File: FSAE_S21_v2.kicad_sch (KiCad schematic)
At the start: 77 parts

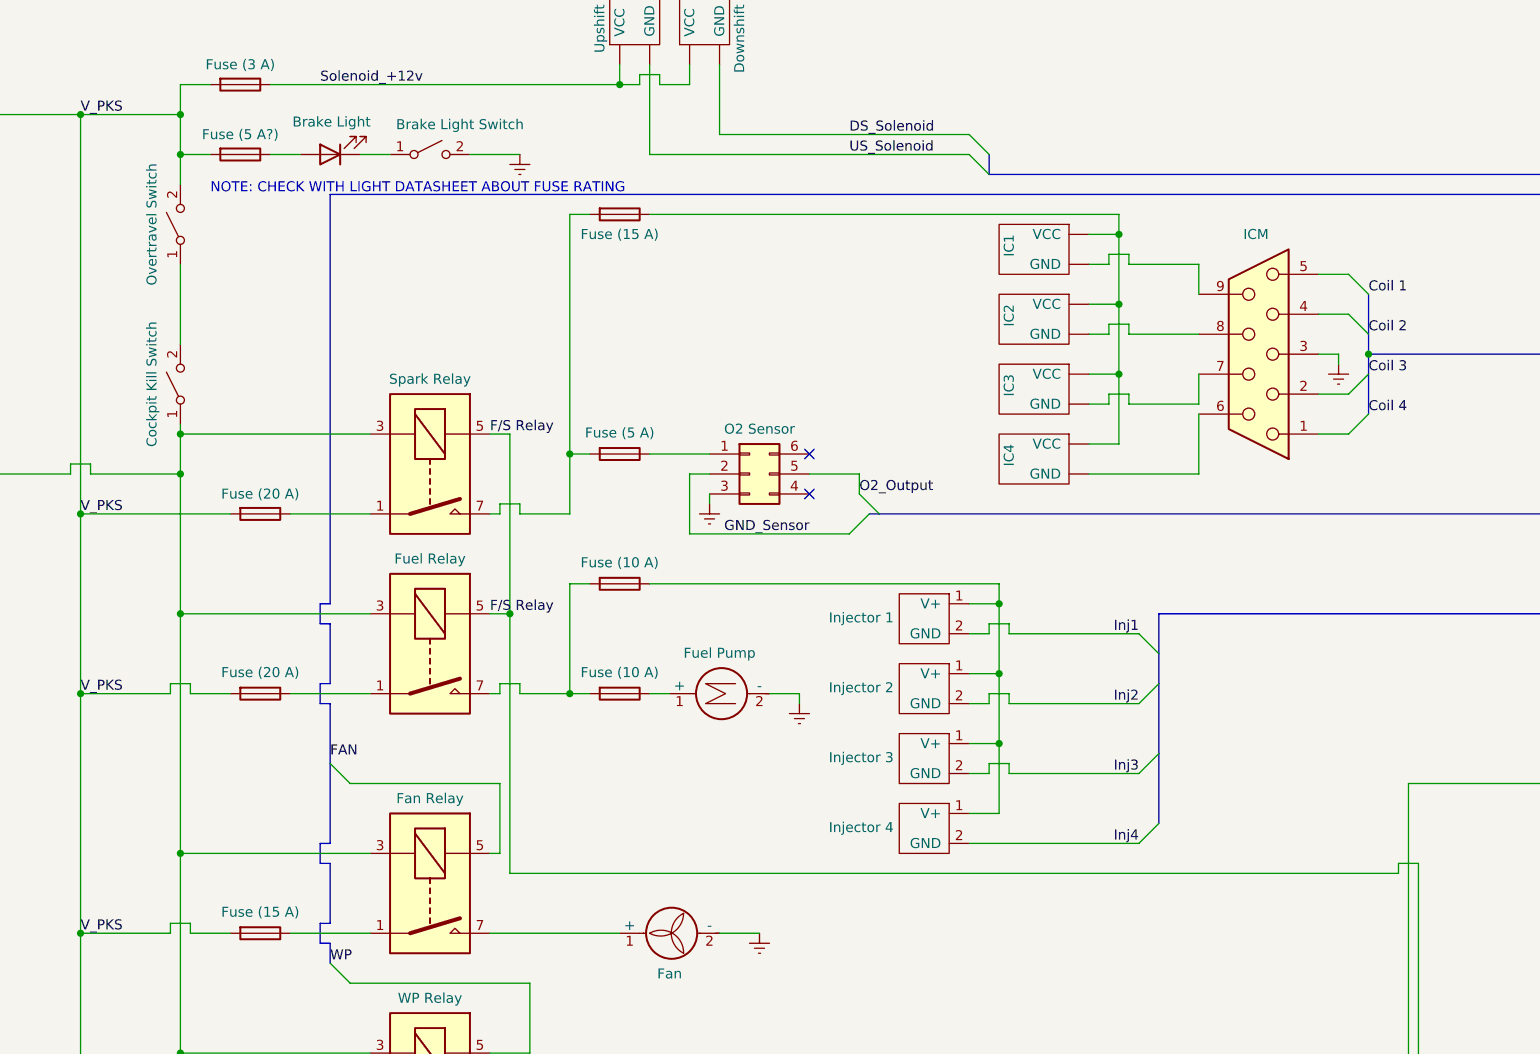
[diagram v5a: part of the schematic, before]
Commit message: fixed killswitch wiring
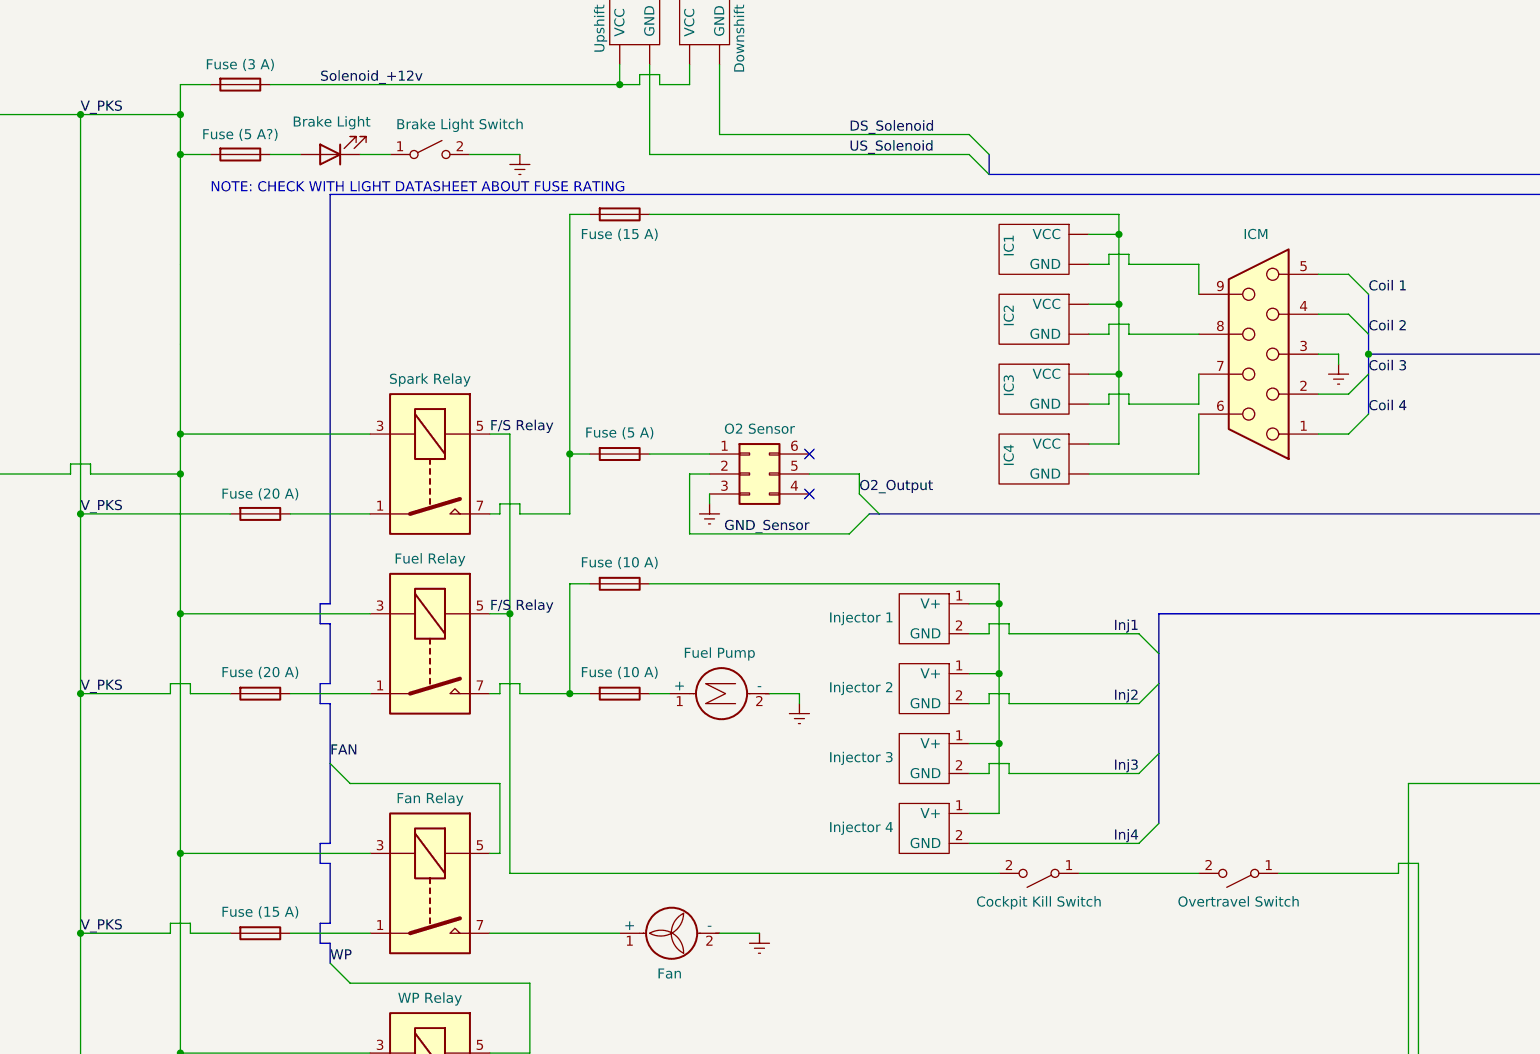
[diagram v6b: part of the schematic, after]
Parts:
- removed SW?: Cockpit Kill Switch, symbol Switch:SW_SPST
- removed SW?: Overtravel Switch, symbol Switch:SW_SPST
- added SW?: Cockpit Kill Switch, symbol Switch:SW_SPST
- added SW?: Overtravel Switch, symbol Switch:SW_SPST
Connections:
- net V_PKS is gone; now on net V_CKS: F?.2, F?.2, F?.2, F?.2, F?.2, F?.2, F?.2, F?.2, F?.2, K?.1, SW?.2 (B)
- net F/S Relay: now also SW?.1 (A), SW?.2 (B)
- new net: F?.1, U?.~ (VCC), U?.~ (VCC), U?.~ (VCC), U?.~ (VCC)
- new net: SW?.1 (A), SW?.2 (B)
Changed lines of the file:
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@@
     (stroke (width 0) (type default) (color 0 0 0 0))
   )
+  (wire (pts (xy 218.44 127) (xy 233.68 127))
+    (stroke (width 0) (type default) (color 0 0 0 0))
+  )
   (wire (pts (xy 403.86 43.18) (xy 417.83 43.18))
     (stroke (width 0) (type default) (color 0 0 0 0))
@@
     (stroke (width 0) (type default) (color 0 0 0 0))
   )
+  (wire (pts (xy 243.84 127) (xy 259.08 127))
+    (stroke (width 0) (type default) (color 0 0 0 0))
+  )
   (wire (pts (xy 441.96 58.42) (xy 441.96 62.23))
     (stroke (width 0) (type default) (color 0 0 0 0))
@@
     (stroke (width 0) (type default) (color 0 0 0 0))
   )
-  (wire (pts (xy 146.05 127) (xy 259.08 127))
+  (wire (pts (xy 146.05 127) (xy 208.28 127))
     (stroke (width 0) (type default) (color 0 0 0 0))
   )
@@
     (stroke (width 0) (type default) (color 0 0 0 0))
   )
-  (wire (pts (xy 539.75 149.86) (xy 548.64 149.86))
+  (wire (pts (xy 104.14 35.56) (xy 104.14 49.53))
     (stroke (width 0) (type default) (color 0 0 0 0))
   )
-  (wire (pts (xy 468.63 62.23) (xy 482.6 62.23))
+  (wire (pts (xy 539.75 149.86) (xy 548.64 149.86))
     (stroke (width 0) (type default) (color 0 0 0 0))
   )
-  (wire (pts (xy 104.14 35.56) (xy 104.14 39.37))
+  (wire (pts (xy 468.63 62.23) (xy 482.6 62.23))
     (stroke (width 0) (type default) (color 0 0 0 0))
   )
@@
     (stroke (width 0) (type default) (color 0 0 0 0))
   )
-  (wire (pts (xy 104.14 71.12) (xy 104.14 69.85))
+  (wire (pts (xy 104.14 59.69) (xy 104.14 71.12))
     (stroke (width 0) (type default) (color 0 0 0 0))
   )
@@
     (pin "2")
   )
-  (symbol (lib_id "Switch:SW_SPST") (at 104.14 64.77 90) (unit 1)
-    (in_bom yes) (on_board yes)
-    (property "Reference" "SW?" (id 0) (at 98.171 64.77 0)
-      (effects (font (size 1.27 1.27)) hide)
-    )
-    (property "Value" "Cockpit Kill Switch" (id 1) (at 100.5078 64.77 0))
-    (property "Footprint" "" (id 2) (at 104.14 64.77 0)
-      (effects (font (size 1.27 1.27)) hide)
-    )
-    (property "Datasheet" "~" (id 3) (at 104.14 64.77 0)
-      (effects (font (size 1.27 1.27)) hide)
-    )
-    (pin "1")
-    (pin "2")
-  )
-  (symbol (lib_id "Switch:SW_SPST") (at 104.14 44.45 90) (unit 1)
-    (in_bom yes) (on_board yes)
-    (property "Reference" "SW?" (id 0) (at 98.171 44.45 0)
-      (effects (font (size 1.27 1.27)) hide)
-    )
-    (property "Value" "Overtravel Switch" (id 1) (at 100.5078 44.45 0))
-    (property "Footprint" "" (id 2) (at 104.14 44.45 0)
-      (effects (font (size 1.27 1.27)) hide)
-    )
-    (property "Datasheet" "~" (id 3) (at 104.14 44.45 0)
-      (effects (font (size 1.27 1.27)) hide)
-    )
-    (pin "1")
-    (pin "2")
-  )
   (symbol (lib_id "Device:LED") (at 123.19 35.56 180) (unit 1)
     (in_bom yes) (on_board yes)
@@
     (pin "2")
   )
+  (symbol (lib_id "Switch:SW_SPST") (at 213.36 127 180) (unit 1)
+    (in_bom yes) (on_board yes)
+    (property "Reference" "SW?" (id 0) (at 213.36 132.969 0)
+      (effects (font (size 1.27 1.27)) hide)
+    )
+    (property "Value" "Cockpit Kill Switch" (id 1) (at 213.36 130.6322 0))
+    (property "Footprint" "" (id 2) (at 213.36 127 0)
+      (effects (font (size 1.27 1.27)) hide)
+    )
+    (property "Datasheet" "~" (id 3) (at 213.36 127 0)
+      (effects (font (size 1.27 1.27)) hide)
+    )
+    (pin "1")
+    (pin "2")
+  )
   (symbol (lib_id "Device:IC") (at 205.74 66.04 270) (unit 1)
     (in_bom yes) (on_board yes)
@@
     (pin "9")
   )
+  (symbol (lib_id "Switch:SW_SPST") (at 238.76 127 180) (unit 1)
+    (in_bom yes) (on_board yes)
+    (property "Reference" "SW?" (id 0) (at 238.76 132.969 0)
+      (effects (font (size 1.27 1.27)) hide)
+    )
+    (property "Value" "Overtravel Switch" (id 1) (at 238.76 130.6322 0))
+    (property "Footprint" "" (id 2) (at 238.76 127 0)
+      (effects (font (size 1.27 1.27)) hide)
+    )
+    (property "Datasheet" "~" (id 3) (at 238.76 127 0)
+      (effects (font (size 1.27 1.27)) hide)
+    )
+    (pin "1")
+    (pin "2")
+  )
   (symbol (lib_id "Relay:SILxx-1Axx-71x") (at 135.89 76.2 270) (unit 1)
     (in_bom yes) (on_board yes)
@@
       (reference "SW?") (unit 1) (value "Brake Light Switch") (footprint "")
     )
-    (path "/00000000-0000-0000-0000-00006037c23a"
-      (reference "SW?") (unit 1) (value "Cockpit Kill Switch") (footprint "")
-    )
-    (path "/00000000-0000-0000-0000-00006037c880"
-      (reference "SW?") (unit 1) (value "Overtravel Switch") (footprint "")
-    )
     (path "/09827712-ae01-4576-8d4a-5c24f2f142d4"
       (reference "SW?") (unit 1) (value "Datalog Button") (footprint "")
     )
+    (path "/0b8034d7-c110-4187-b7e1-2952bbb68d07"
+      (reference "SW?") (unit 1) (value "Cockpit Kill Switch") (footprint "")
+    )
     (path "/481b68e8-b9de-4f54-a811-464101e73c9c"
       (reference "SW?") (unit 1) (value "Upshift Button") (footprint "")
@@
       (reference "SW?") (unit 1) (value "Starter Button") (footprint "")
     )
+    (path "/6e3c3257-8ec7-454b-8583-06e57d9f4550"
+      (reference "SW?") (unit 1) (value "Overtravel Switch") (footprint "")
+    )
     (path "/f0a0ce9c-368e-4400-b607-2ed64fcfd307"

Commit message: idk what i changed
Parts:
- added J?: USB Adapter (W/ Terminating), symbol Connector_Generic:Conn_01x02
- added J?: MicroSquirt, symbol Connector_Generic:Conn_01x02
- added J?: IMU, symbol Connector_Generic:Conn_01x02
- added J?: Megasquirt (w/ terminating), symbol Connector_Generic:Conn_01x02
- F?: value Fuse (5 A?) -> Fuse (1 A)
- J?: value Raspberry Pi/Buck Converter -> Raspberry Pi Buck Converter
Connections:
- net CANH: no longer J?.2 (Pin_2)
- net CANL: no longer J?.1 (Pin_1)
- new net: F?.1, U?.~ (VCC), U?.~ (VCC), U?.~ (VCC), U?.~ (VCC)
- new net: J?.1 (Pin_1), J?.1 (Pin_1), J?.1 (Pin_1), J?.1 (Pin_1)
- new net: J?.2 (Pin_2), J?.2 (Pin_2), J?.2 (Pin_2), J?.2 (Pin_2)
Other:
- note added: "CANBUS TOPOLOGY"
- note added: "NOTE: SWAP 3 AND 4 FOR FUEL/SPARK"

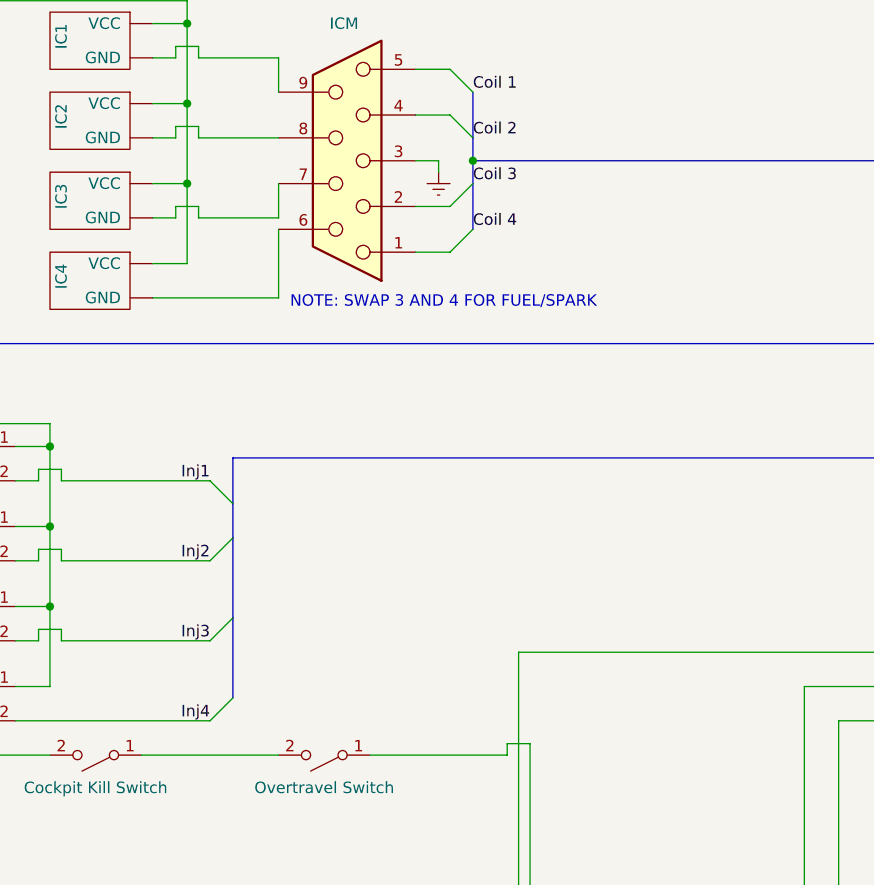
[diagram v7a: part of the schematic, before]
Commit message: swapped fuel/spark 3 and 4
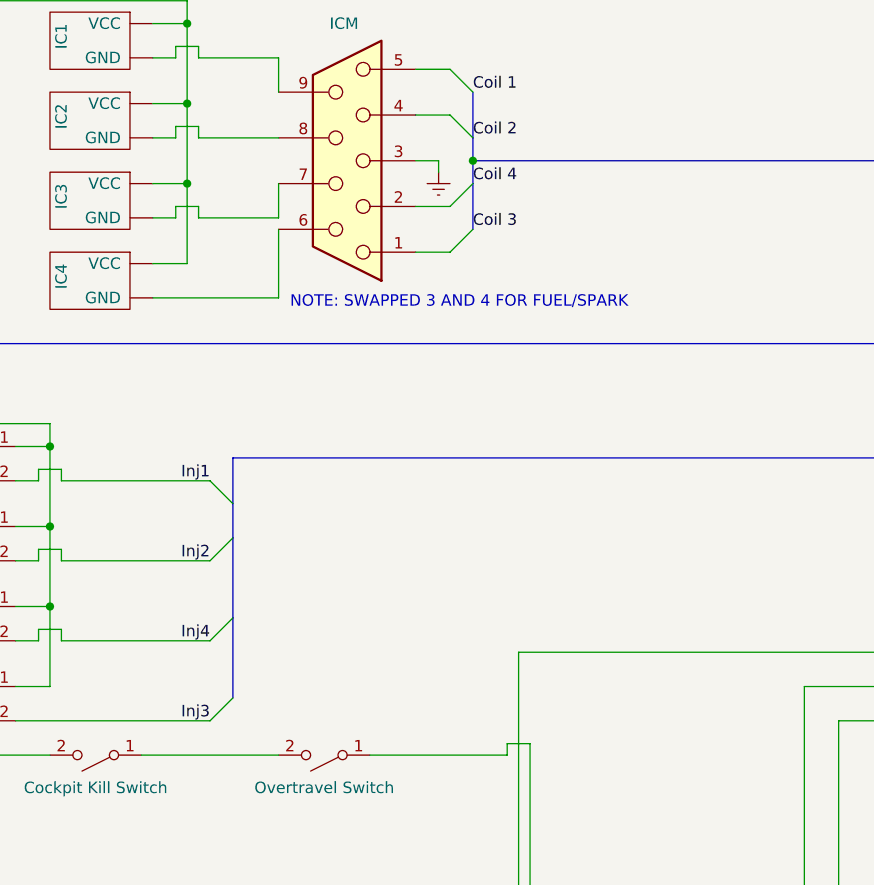
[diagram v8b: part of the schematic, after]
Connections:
- net Inj3: now also U?.2 (GND); no longer U?.2 (GND)
- net Inj4: now also U?.2 (GND); no longer U?.2 (GND)
- new net: F?.1, U?.~ (VCC), U?.~ (VCC), U?.~ (VCC), U?.~ (VCC)
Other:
- note added: "NOTE: SWAPPED 3 AND 4 FOR FUEL/SPARK"
- note removed: "NOTE: SWAP 3 AND 4 FOR FUEL/SPARK"
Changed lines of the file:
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@@
     (effects (font (size 1.27 1.27)) (justify left bottom))
   )
-  (text "NOTE: SWAP 3 AND 4 FOR FUEL/SPARK\n" (at 234.95 77.47 0)
+  (text "NOTE: SWAPPED 3 AND 4 FOR FUEL/SPARK" (at 234.95 77.47 0)
     (effects (font (size 1.27 1.27)) (justify left bottom))
   )
@@
     (effects (font (size 1.27 1.27)) (justify left bottom))
   )
-  (label "Inj4" (at 226.06 123.19 180)
+  (label "Inj3" (at 226.06 123.19 180)
     (effects (font (size 1.27 1.27)) (justify right bottom))
   )
@@
     (effects (font (size 1.27 1.27)) (justify right bottom))
   )
-  (label "Coil 3" (at 255.27 63.5 0)
+  (label "Coil 4" (at 255.27 63.5 0)
     (effects (font (size 1.27 1.27)) (justify left bottom))
   )
@@
     (effects (font (size 1.27 1.27)) (justify left bottom))
   )
-  (label "Coil 4" (at 255.27 68.58 0)
+  (label "Coil 3" (at 255.27 68.58 0)
     (effects (font (size 1.27 1.27)) (justify left bottom))
   )
@@
     (effects (font (size 0.9906 0.9906)) (justify left bottom))
   )
-  (label "Inj3" (at 226.06 114.3 180)
-    (effects (font (size 1.27 1.27)) (justify right bottom))
-  )
+  (label "Inj4" (at 226.06 114.3 180)
+    (effects (font (size 1.27 1.27)) (justify right bottom))
+  )
